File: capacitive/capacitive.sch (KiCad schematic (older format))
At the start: 86 parts, among them J101 UL, J102 UART, J103 SWD, J104 TX_PADS, J105 RX_PAD, J106 POWER, J107 UR, J108 LL, J109 LR, Q101 RU1C002ZPTCL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

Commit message: Change scale size and finish relayout
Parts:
- removed C122: DNP, Capacitors_SMD:C_0603_HandSoldering, symbol C_Small
- removed R116: 0, Resistors_SMD:R_0805_HandSoldering, symbol R_Small
- C109: value 10 nF 2% -> 10 nF 1%
- C123: footprint Capacitors_SMD:C_0805_HandSoldering -> Capacitors_SMD:C_1210_HandSoldering; Mouser 710-885012207016 -> 581-TAJB106K020RNJV
- J103: footprint Socket_Strips:Socket_Strip_Straight_2x03_Pitch2.54mm -> Socket_Strips:Socket_Strip_Straight_2x03_Pitch2.54mm_SMD; Mouser NoPart -> 855-M20-8750342
- J106: footprint Socket_Strips:Socket_Strip_Straight_1x02_Pitch2.54mm -> capacitive:Power_Pads
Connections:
- net +1V65: now also U102.10 (+); no longer U102.12 (+)
- net +5V: now also Q101.2 (S); no longer Q101.3 (D)
- net at C115.1, U104.1 (IN), U104.3 (EN): now also Q101.3 (D); no longer Q101.2 (S)
- net at R106.1, R114.2, TP106.1: now also U102.3 (+)
- net at R126.1, R127.1, TP112.1: now also U102.12 (+); no longer U102.10 (+)
- net at C124.2, R117.2, R119.1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: now also U102.14; no longer U102.8
- net at C124.1, R117.1, R118.2: now also U102.13 (-); no longer U102.9 (-)
- net at C126.2, R121.2: now also U102.9 (-); no longer U102.13 (-)
- net at C127.1, R126.2: now also U102.8; no longer U102.14
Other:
- moved on the sheet: U102C, U102D

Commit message: Swap out MOSFET to RU1C001ZP
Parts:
- Q101: Mouser 755-RU1C002ZPTCL -> 755-RU1C001ZPTL
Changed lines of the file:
@@
 F 2 "capacitive:Rohm_UMT3F" H 3250 5750 50  0001 C CNN
 F 3 "" H 3050 5650 50  0001 C CNN
-F 4 "755-RU1C002ZPTCL" H 3050 5650 60  0001 C CNN "Mouser"
+F 4 "755-RU1C001ZPTL" H 3050 5650 60  0001 C CNN "Mouser"
 	1    3050 5650
 	1    0    0    1

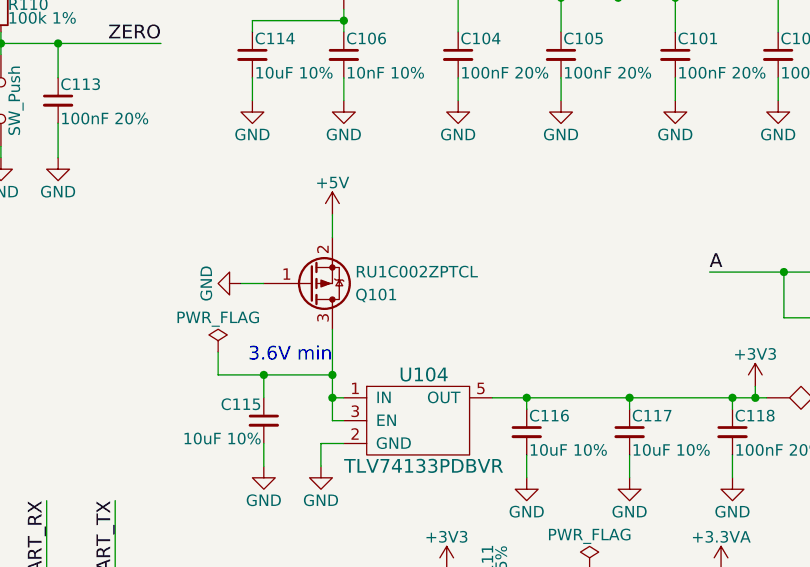
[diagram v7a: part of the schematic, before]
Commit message: Fix reverse voltage MOSFET probably
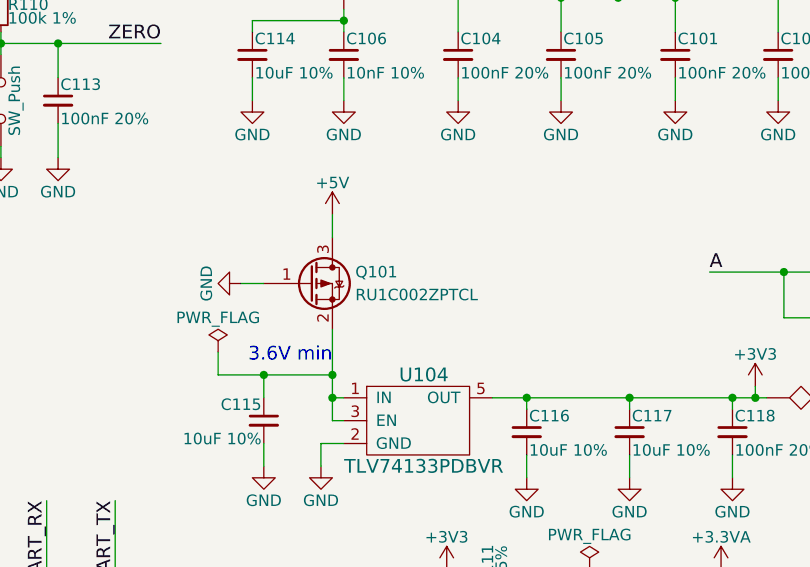
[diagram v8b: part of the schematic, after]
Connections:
- net +5V: now also Q101.3 (D); no longer Q101.2 (S)
- net at C115.1, U104.1 (IN), U104.3 (EN): now also Q101.2 (S); no longer Q101.3 (D)
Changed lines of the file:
@@
 F 4 "755-RU1C001ZPTL" H 3050 5650 60  0001 C CNN "Mouser"
 	1    3050 5650
-	1    0    0    1
+	1    0    0    -1
 $EndComp
 $Comp
